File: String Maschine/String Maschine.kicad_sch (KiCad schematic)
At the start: 52 parts, among them J1 Vin, J2 VGG, J3 VOut, J4 Vin, J5 CTLS, SW1 FBACK, SW2 NOISE, SW3 FBACK, U1 v2164, U2 LM324, U3 Pentanoise, U5 MN3209

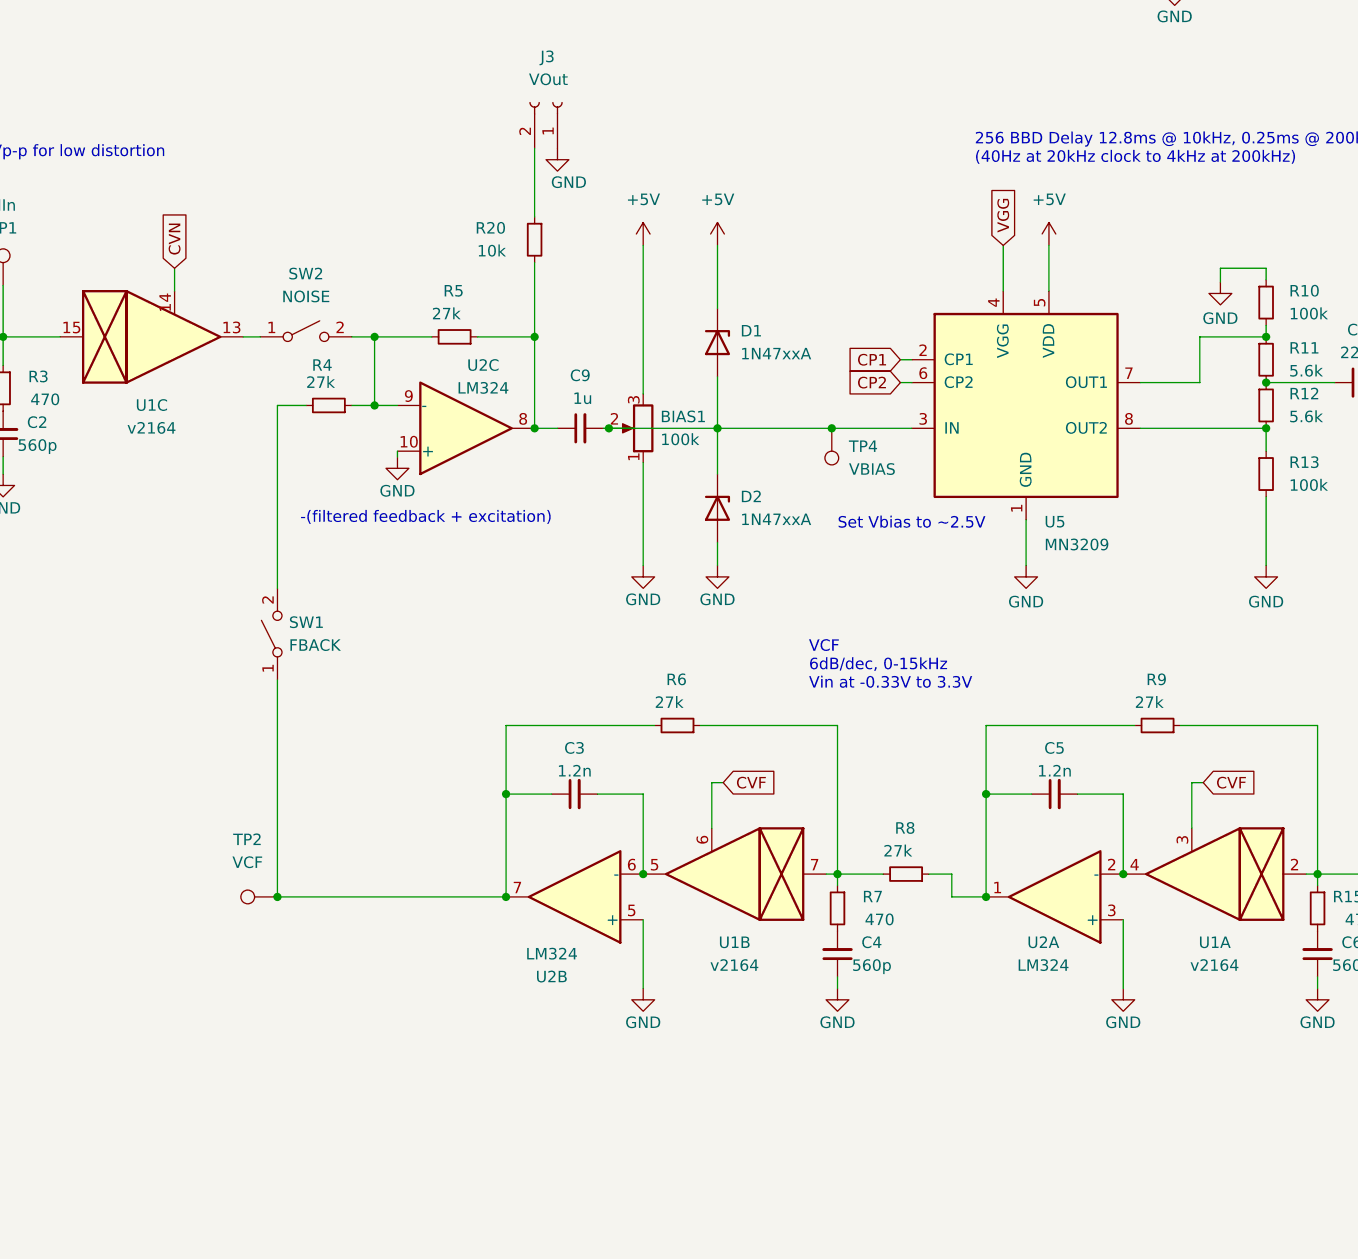
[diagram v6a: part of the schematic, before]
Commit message: String Maschine controller - fix broken symbols
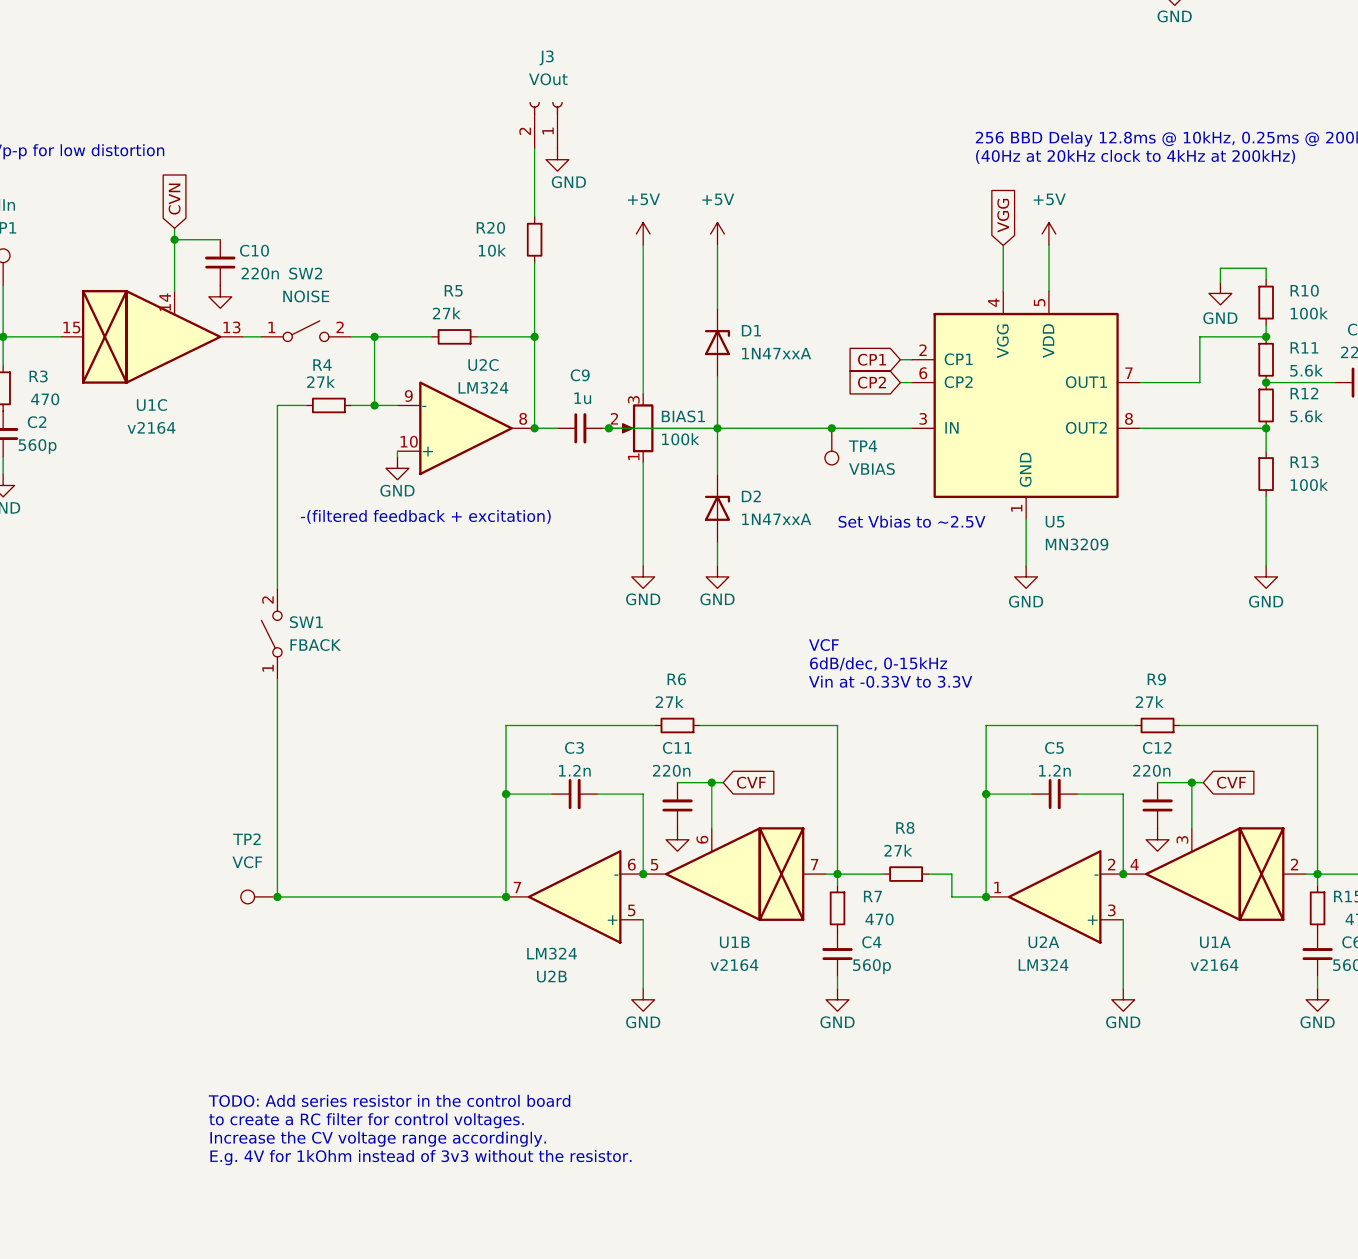
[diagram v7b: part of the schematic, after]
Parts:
- added C10, C11, C12: 220n, Capacitor_THT:C_Rect_L7.0mm_W4.5mm_P5.00mm, symbol Device:C_Small
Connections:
- net CVF: now also C11.2, C12.2
- net CVN: now also C10.2
- net GND: now also C10.1, C11.1, C12.1
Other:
- note added: "TODO: Add series resistor in the control board to create a RC filter for control voltages. Increase the CV voltage range accordingly. E.g. 4V for 1kOhm instead of 3v3 without the resistor."

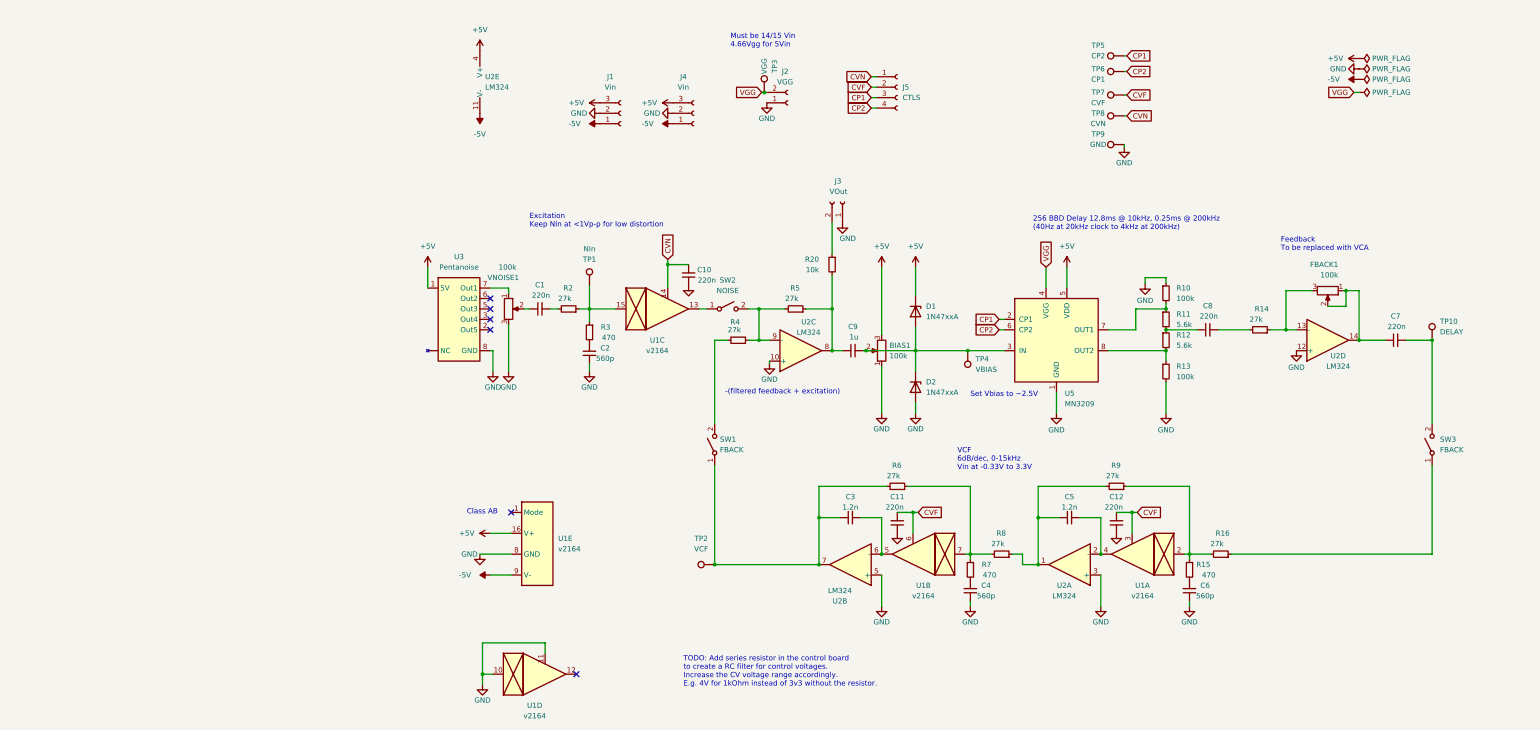
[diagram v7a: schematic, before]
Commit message: String Maschine - Add simulations and add VCA for controlling the feedback loop
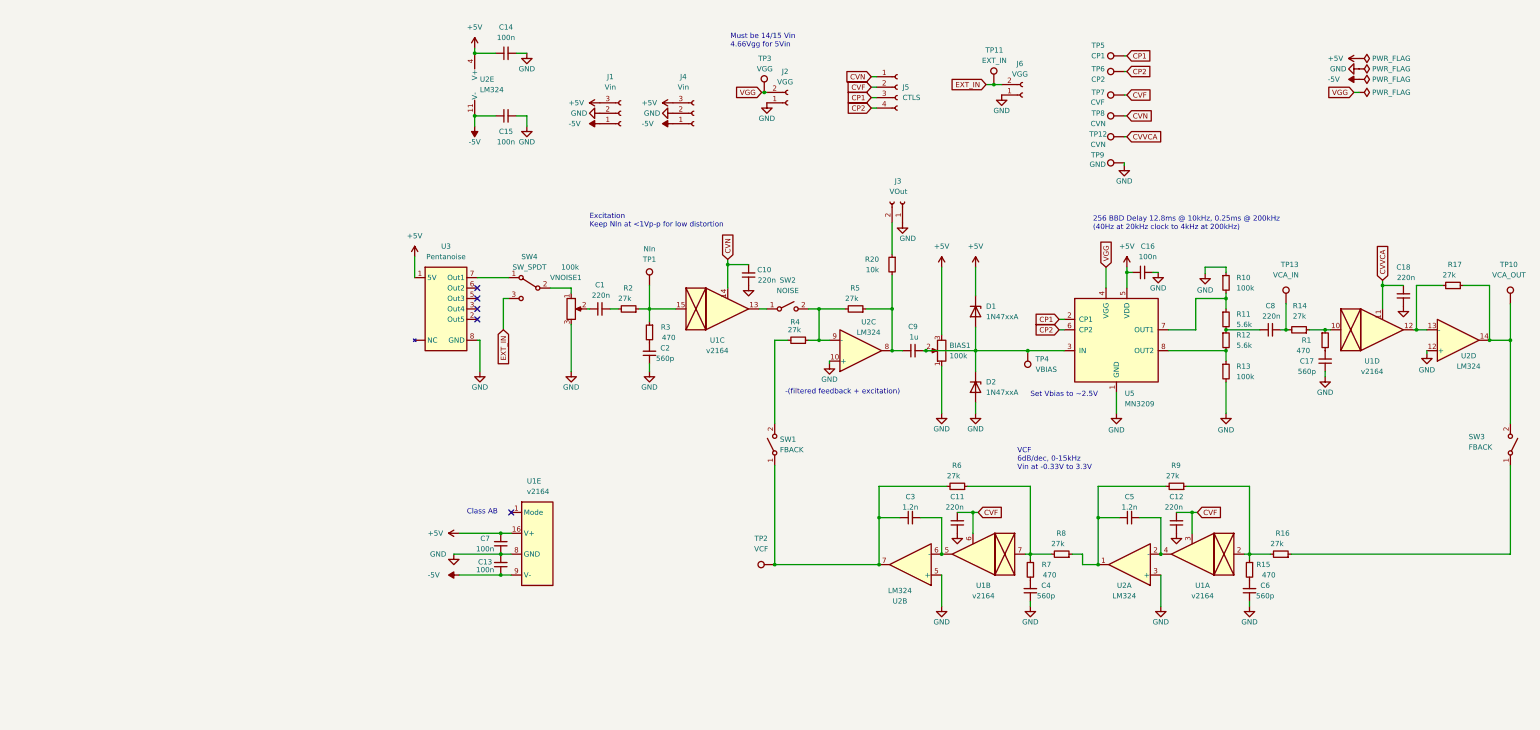
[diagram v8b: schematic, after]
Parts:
- removed FBACK1: 100k, Connector_JST:JST_PH_B3B-PH-K_1x03_P2.00mm_Vertical, symbol Device:R_Potentiometer
- added C13, C14, C15, C16: 100n, Capacitor_THT:C_Rect_L7.0mm_W4.5mm_P5.00mm, symbol Device:C_Small
- added C17: 560p, Capacitor_THT:C_Rect_L7.0mm_W4.5mm_P5.00mm, symbol Device:C_Small
- added C18: 220n, Capacitor_THT:C_Rect_L7.0mm_W4.5mm_P5.00mm, symbol Device:C_Small
- added J6: VGG, Connector_PinHeader_2.54mm:PinHeader_1x02_P2.54mm_Vertical, symbol Connector:Conn_01x02_Female
- added R1: 470, Resistor_THT:R_Axial_DIN0207_L6.3mm_D2.5mm_P10.16mm_Horizontal, symbol Device:R_Small
- added R17: 27k, Resistor_THT:R_Axial_DIN0207_L6.3mm_D2.5mm_P10.16mm_Horizontal, symbol Device:R_Small
- added SW4: SW_SPDT, symbol Switch:SW_SPDT
- added TP11: EXT_IN, TestPoint:TestPoint_Pad_D1.0mm, symbol Connector:TestPoint
- added TP12: CVN, TestPoint:TestPoint_Pad_D1.0mm, symbol Connector:TestPoint
- added TP13: VCA_IN, TestPoint:TestPoint_Pad_D1.0mm, symbol Connector:TestPoint
- C7: value 220n -> 100n
- TP10: value DELAY -> VCA_OUT
- TP5: value CP2 -> CP1
- TP6: value CP1 -> CP2
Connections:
- net +5V: now also C7.2, C14.1, C16.1
- net -5V: now also C13.1, C15.1
- net GND: now also C7.1, C13.2, C14.2, C15.2, C16.2, C17.1, C18.1, J6.1 (Pin_1); no longer U1.10, U1.11
- net at SW3.2 (B), TP10.1: now also U2.14, R17.1; no longer C7.2
- net at U1.12: now also U2.13 (-), R17.2
- net at R14.1: now also U1.10, R1.1; no longer U2.13 (-)
- net at U3.7 (Out1): now also SW4.1 (A); no longer VNOISE1.1
- net at C8.2, R14.2: now also TP13.1
- new net: C17.2, R1.2
- new net: SW4.2 (B), VNOISE1.1
- new net CVVCA: C18.2, TP12.1, U1.11
- new net EXT_IN: J6.2 (Pin_2), SW4.3 (C), TP11.1
- no-connect marks 6 -> 5
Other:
- note removed: "Feedback To be replaced with VCA"
- note removed: "TODO: Add series resistor in the control board to create a RC filter for control voltages. Increase the CV voltage range accordingly. E.g. 4V for 1kOhm instead of 3v3 without the resistor."
- moved on the sheet: BIAS1, C1, C10, C11, C12, C2, C3, C4, C5, C6, C8, C9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
